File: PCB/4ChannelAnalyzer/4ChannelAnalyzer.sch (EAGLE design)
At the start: 19 parts, among them U1 ADS1015IDGST, U2 ADS1015IDGST, U3 LM1117MP-3.3, X3 MINI-USB-32005-301

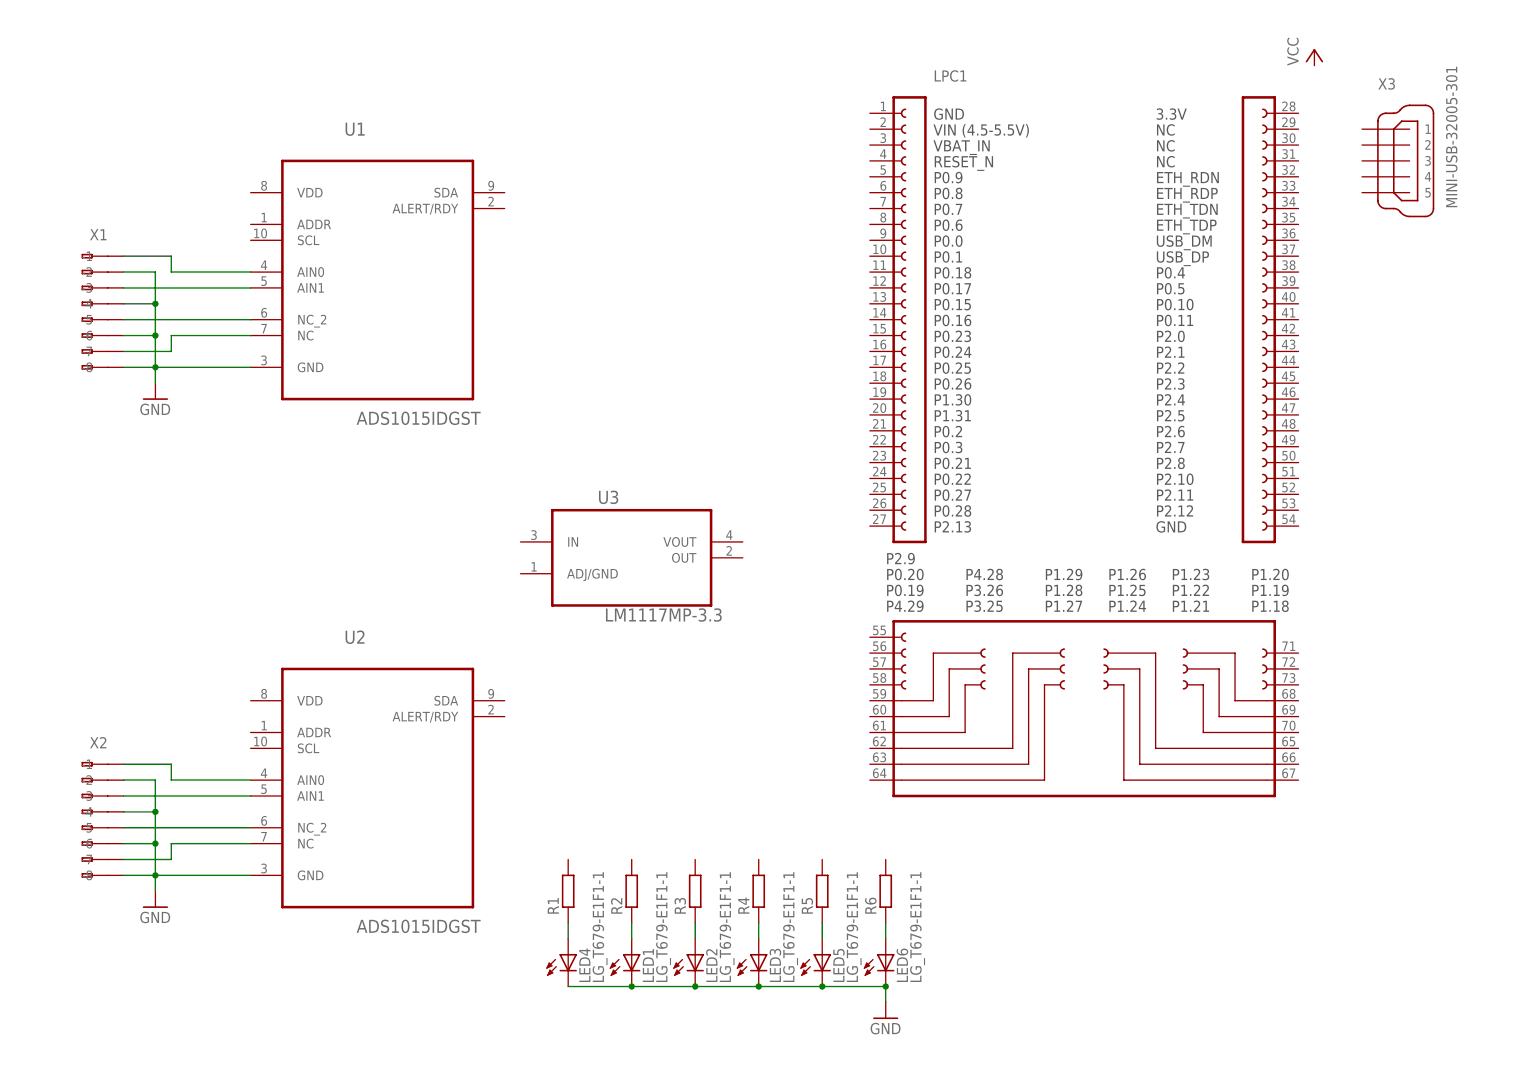
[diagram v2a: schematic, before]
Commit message: adc's ready signal pins / USB connector
connected adc's ready signal pins to uC and wired USB connector
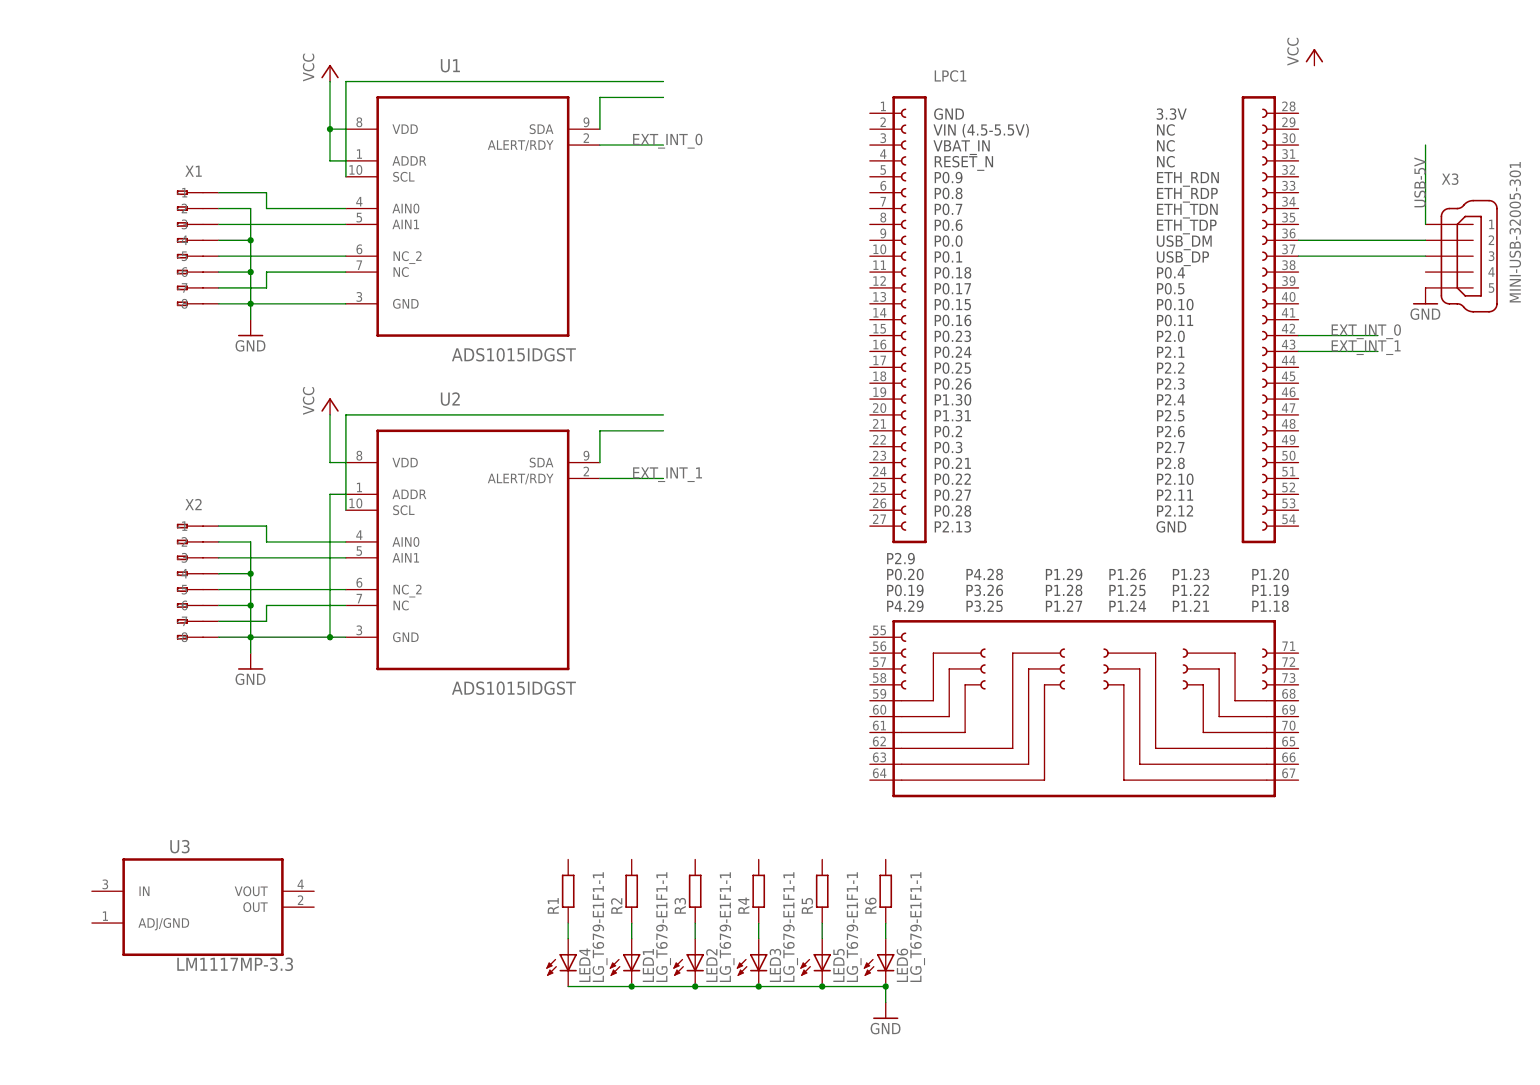
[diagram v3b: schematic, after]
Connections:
- new net EXT_INT_0: LPC1.42, U1.ALERT/RDY
- new net EXT_INT_1: LPC1.43, U2.ALERT/RDY
- new net N$15: U1.SCL
- new net N$16: U1.SDA
- new net N$17: U2.SCL
- new net N$18: U2.SDA
- new net N$19: LPC1.36, X3.2
- new net N$20: LPC1.37, X3.3
- new net USB-5V: X3.1
- new net VCC: U1.ADDR, U1.VDD, U2.VDD
- net GND: now also U2.ADDR, X3.5
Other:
- moved on the sheet: U1, U2, U3, X1, X2, X3

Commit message: Wired LED signals.
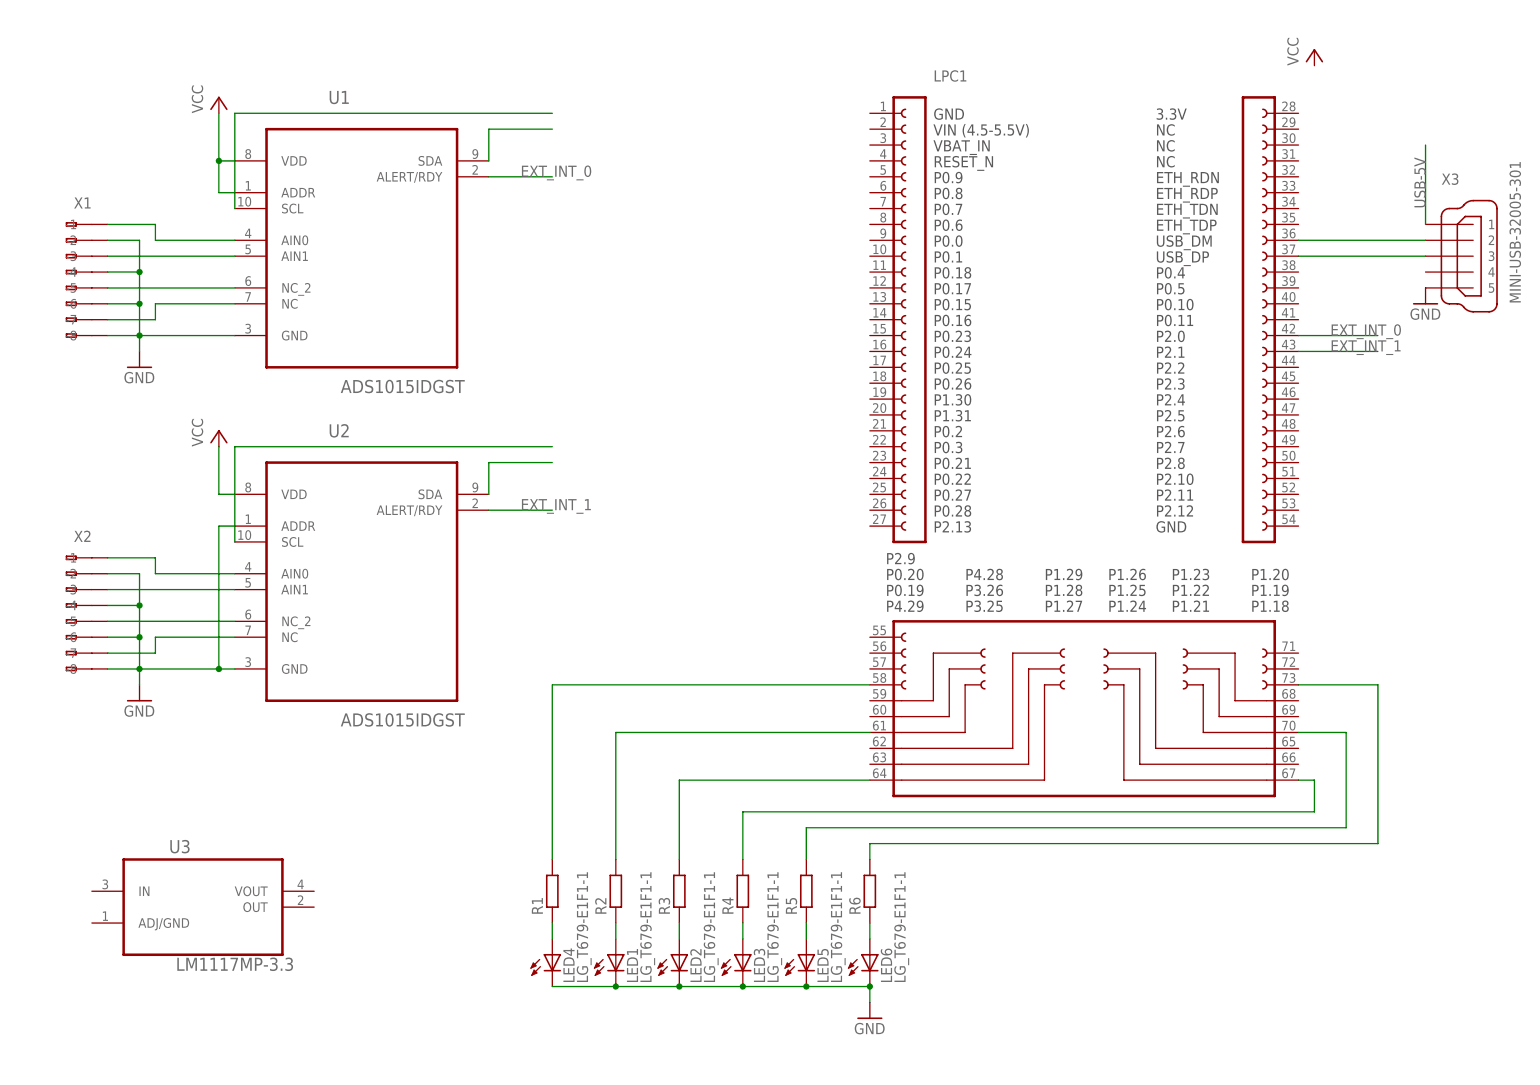
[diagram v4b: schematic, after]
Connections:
- new net N$21: LPC1.58, R1.2
- new net N$22: LPC1.61, R2.2
- new net N$23: LPC1.64, R3.2
- new net N$24: LPC1.67, R4.2
- new net N$25: LPC1.70, R5.2
- new net N$26: LPC1.73, R6.2
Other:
- moved on the sheet: LED1, LED2, LED3, LED4, LED5, LED6, R1, R2, R3, R4, R5, R6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

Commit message: Conected ADC to uC, wired ADC to connector (in PCB)
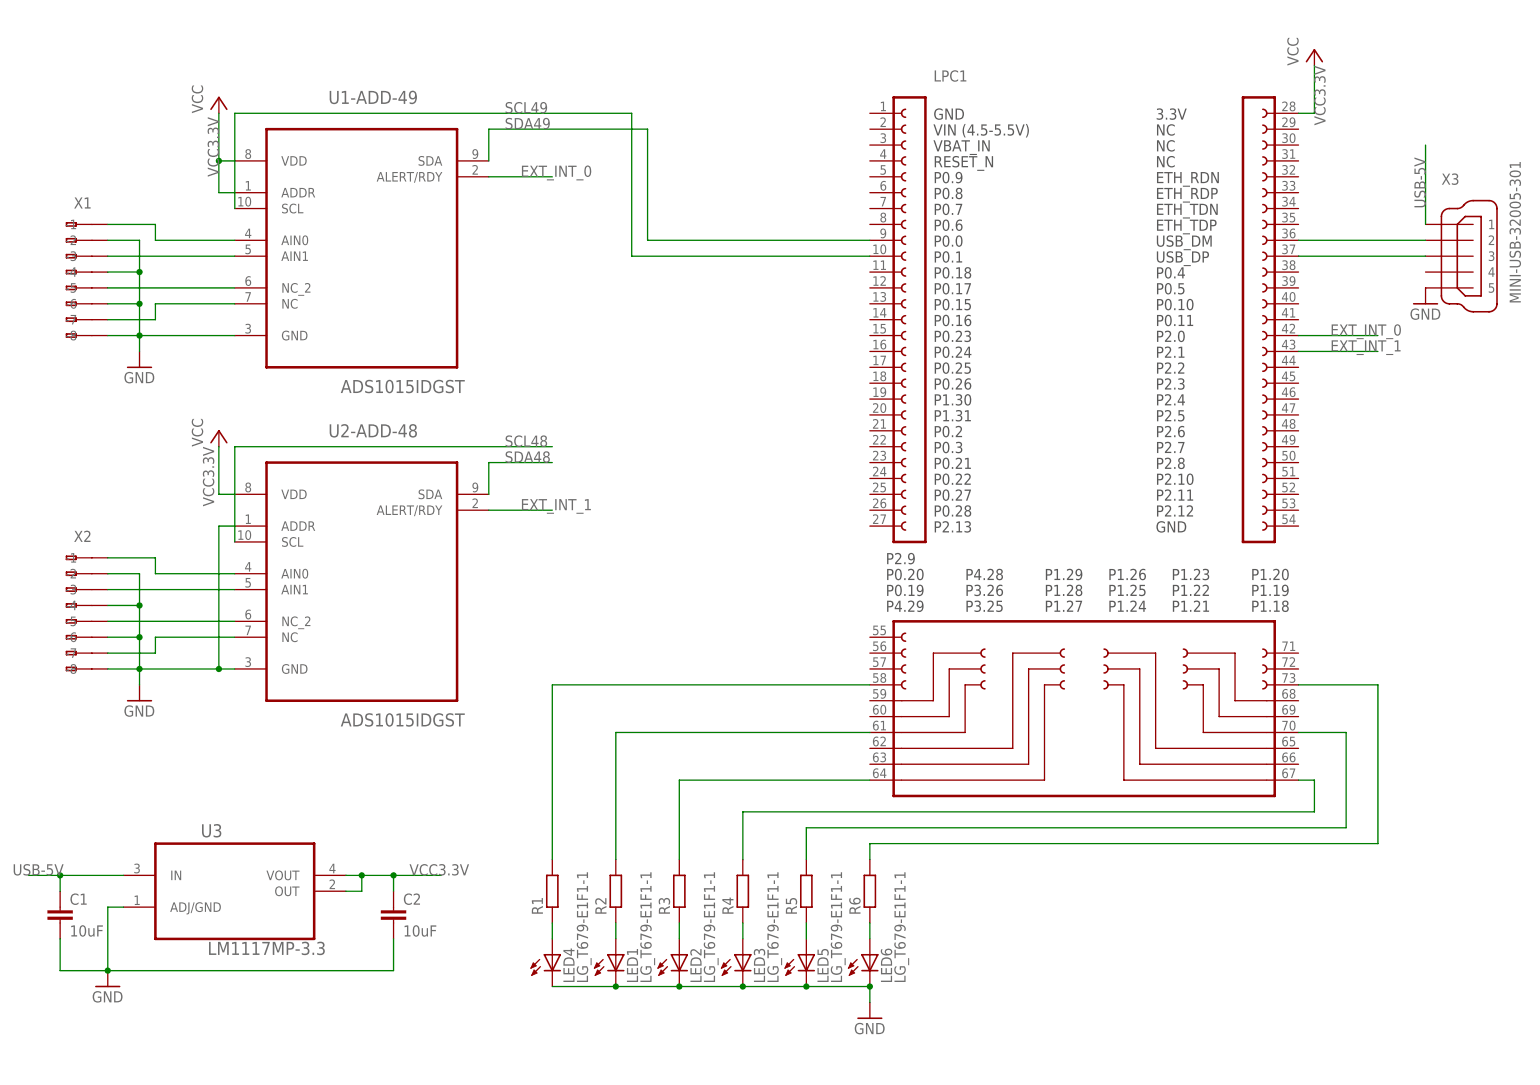
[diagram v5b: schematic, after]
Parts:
- added C1, C2: 10uF, rcl:C-EUC0805
- renumbered U1 to U1-ADD-49, U2 to U2-ADD-48
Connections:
- net N$17 renamed SCL48
- net N$18 renamed SDA48
- removed net N$15: U1-ADD-49.SCL
- removed net N$16: U1-ADD-49.SDA
- removed net VCC: U1-ADD-49.ADDR, U1-ADD-49.VDD, U2-ADD-48.VDD
- new net SCL49: LPC1.10, U1-ADD-49.SCL
- new net SDA49: LPC1.9, U1-ADD-49.SDA
- new net VCC3.3V: C2.1, LPC1.28, U1-ADD-49.ADDR, U1-ADD-49.VDD, U2-ADD-48.VDD, U3.OUT, U3.VOUT
- net GND: now also C1.2, C2.2, U3.ADJ/GND
- net USB-5V: now also C1.1, U3.IN
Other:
- moved on the sheet: U3

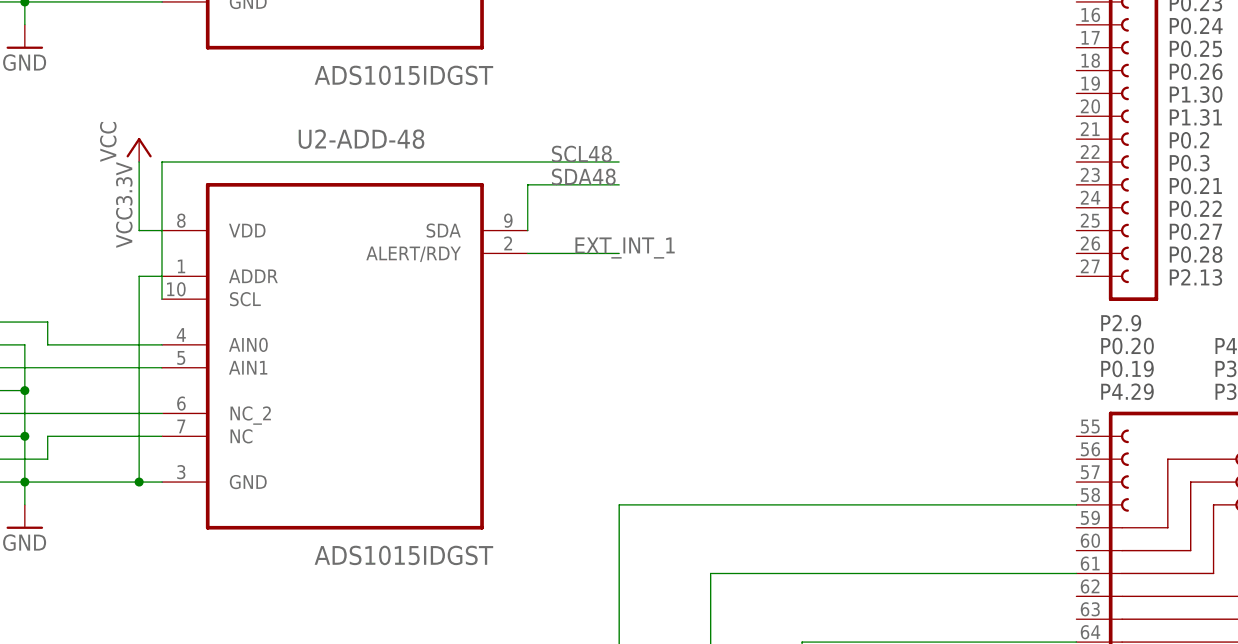
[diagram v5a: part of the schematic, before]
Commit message: Wiring all components (without power supply)
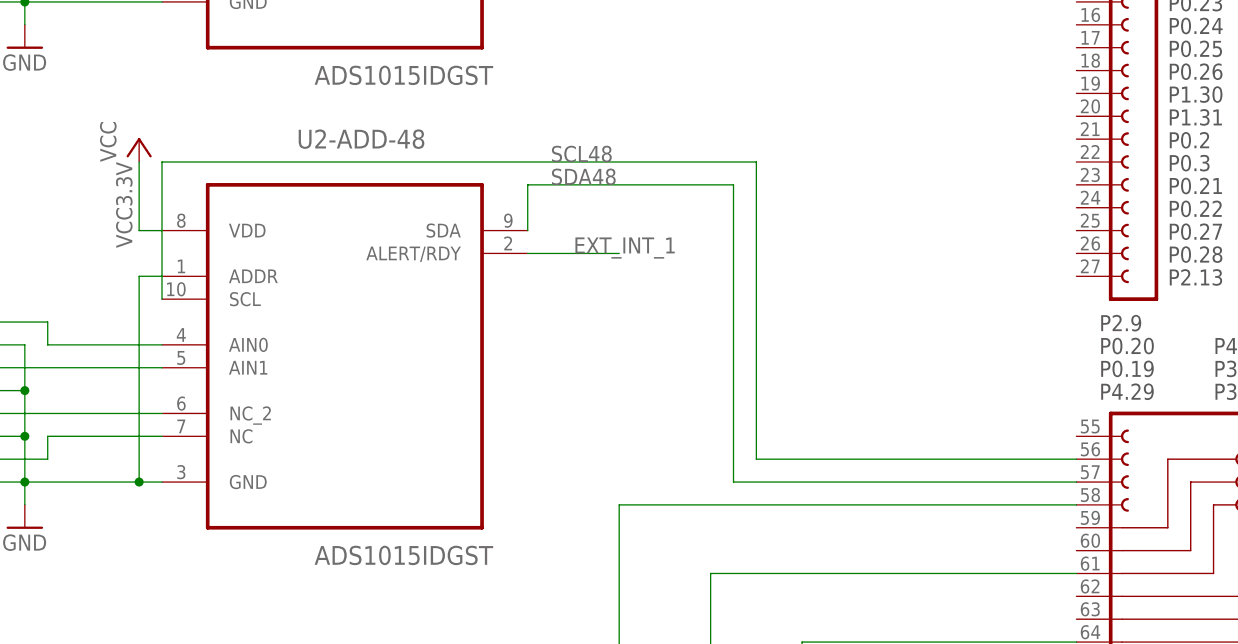
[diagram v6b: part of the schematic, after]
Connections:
- net SCL48: now also LPC1.56
- net SDA48: now also LPC1.57
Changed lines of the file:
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@@
 <pinref part="U2-ADD-48" gate="A" pin="SCL"/>
 <wire x1="48.26" y1="88.9" x2="48.26" y2="104.14" width="0.1524" layer="91"/>
-<wire x1="48.26" y1="104.14" x2="99.06" y2="104.14" width="0.1524" layer="91"/>
+<wire x1="48.26" y1="104.14" x2="114.3" y2="104.14" width="0.1524" layer="91"/>
 <label x="91.44" y="104.14" size="1.778" layer="95"/>
+<wire x1="114.3" y1="104.14" x2="114.3" y2="71.12" width="0.1524" layer="91"/>
+<pinref part="LPC1" gate="G$1" pin="56"/>
+<wire x1="114.3" y1="71.12" x2="149.86" y2="71.12" width="0.1524" layer="91"/>
 </segment>
 </net>
@@
 <pinref part="U2-ADD-48" gate="A" pin="SDA"/>
 <wire x1="88.9" y1="96.52" x2="88.9" y2="101.6" width="0.1524" layer="91"/>
-<wire x1="88.9" y1="101.6" x2="99.06" y2="101.6" width="0.1524" layer="91"/>
 <label x="91.44" y="101.6" size="1.778" layer="95"/>
+<wire x1="88.9" y1="101.6" x2="111.76" y2="101.6" width="0.1524" layer="91"/>
+<wire x1="111.76" y1="101.6" x2="111.76" y2="68.58" width="0.1524" layer="91"/>
+<pinref part="LPC1" gate="G$1" pin="57"/>
+<wire x1="111.76" y1="68.58" x2="149.86" y2="68.58" width="0.1524" layer="91"/>
 </segment>
 </net>

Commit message: Wiring sensors connectors.
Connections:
- net GND: now also LPC1.1
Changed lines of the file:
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@@
 <part name="C2" library="rcl" deviceset="C-EU" device="C0805" value="10uF"/>
 <part name="GND5" library="supply1" deviceset="GND" device=""/>
+<part name="GND6" library="supply1" deviceset="GND" device=""/>
 </parts>
 <sheets>
@@
 <instance part="C2" gate="G$1" x="73.66" y="30.48"/>
 <instance part="GND5" gate="1" x="27.94" y="17.78"/>
+<instance part="GND6" gate="1" x="139.7" y="152.4"/>
 </instances>
 <busses>
@@
 <junction x="27.94" y="20.32"/>
 </segment>
+<segment>
+<pinref part="LPC1" gate="G$1" pin="1"/>
+<pinref part="GND6" gate="1" pin="GND"/>
+<wire x1="149.86" y1="157.48" x2="139.7" y2="157.48" width="0.1524" layer="91"/>
+<wire x1="139.7" y1="157.48" x2="139.7" y2="154.94" width="0.1524" layer="91"/>
+</segment>
 </net>

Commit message: Final design of the of the main module PCB
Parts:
- removed LED1, LED2, LED3, LED4, LED5, LED6: LG_T679-E1F1-1, led:LG_T679-E1F1-1
- added J1: (no value), con-amp:MTA07-100
- added R7, R8: 10K, rcl:R-EU_M0805
- R1, R2, R3, R4, R5, R6: value (none) -> 10
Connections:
- net GND: now also J1.7; no longer LED1.C, LED2.C, LED3.C, LED4.C, LED5.C, LED6.C
- net N$2: now also J1.6; no longer LED4.A
- net N$3: now also J1.5; no longer LED1.A
- net N$4: now also J1.4; no longer LED2.A
- net N$5: now also J1.3; no longer LED3.A
- net N$6: now also J1.2; no longer LED5.A
- net N$7: now also J1.1; no longer LED6.A
- net SCL49: now also R8.1
- net SDA49: now also R7.1
- net VCC3.3V: now also R7.2, R8.2
